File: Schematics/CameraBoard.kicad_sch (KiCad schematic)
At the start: 0 parts

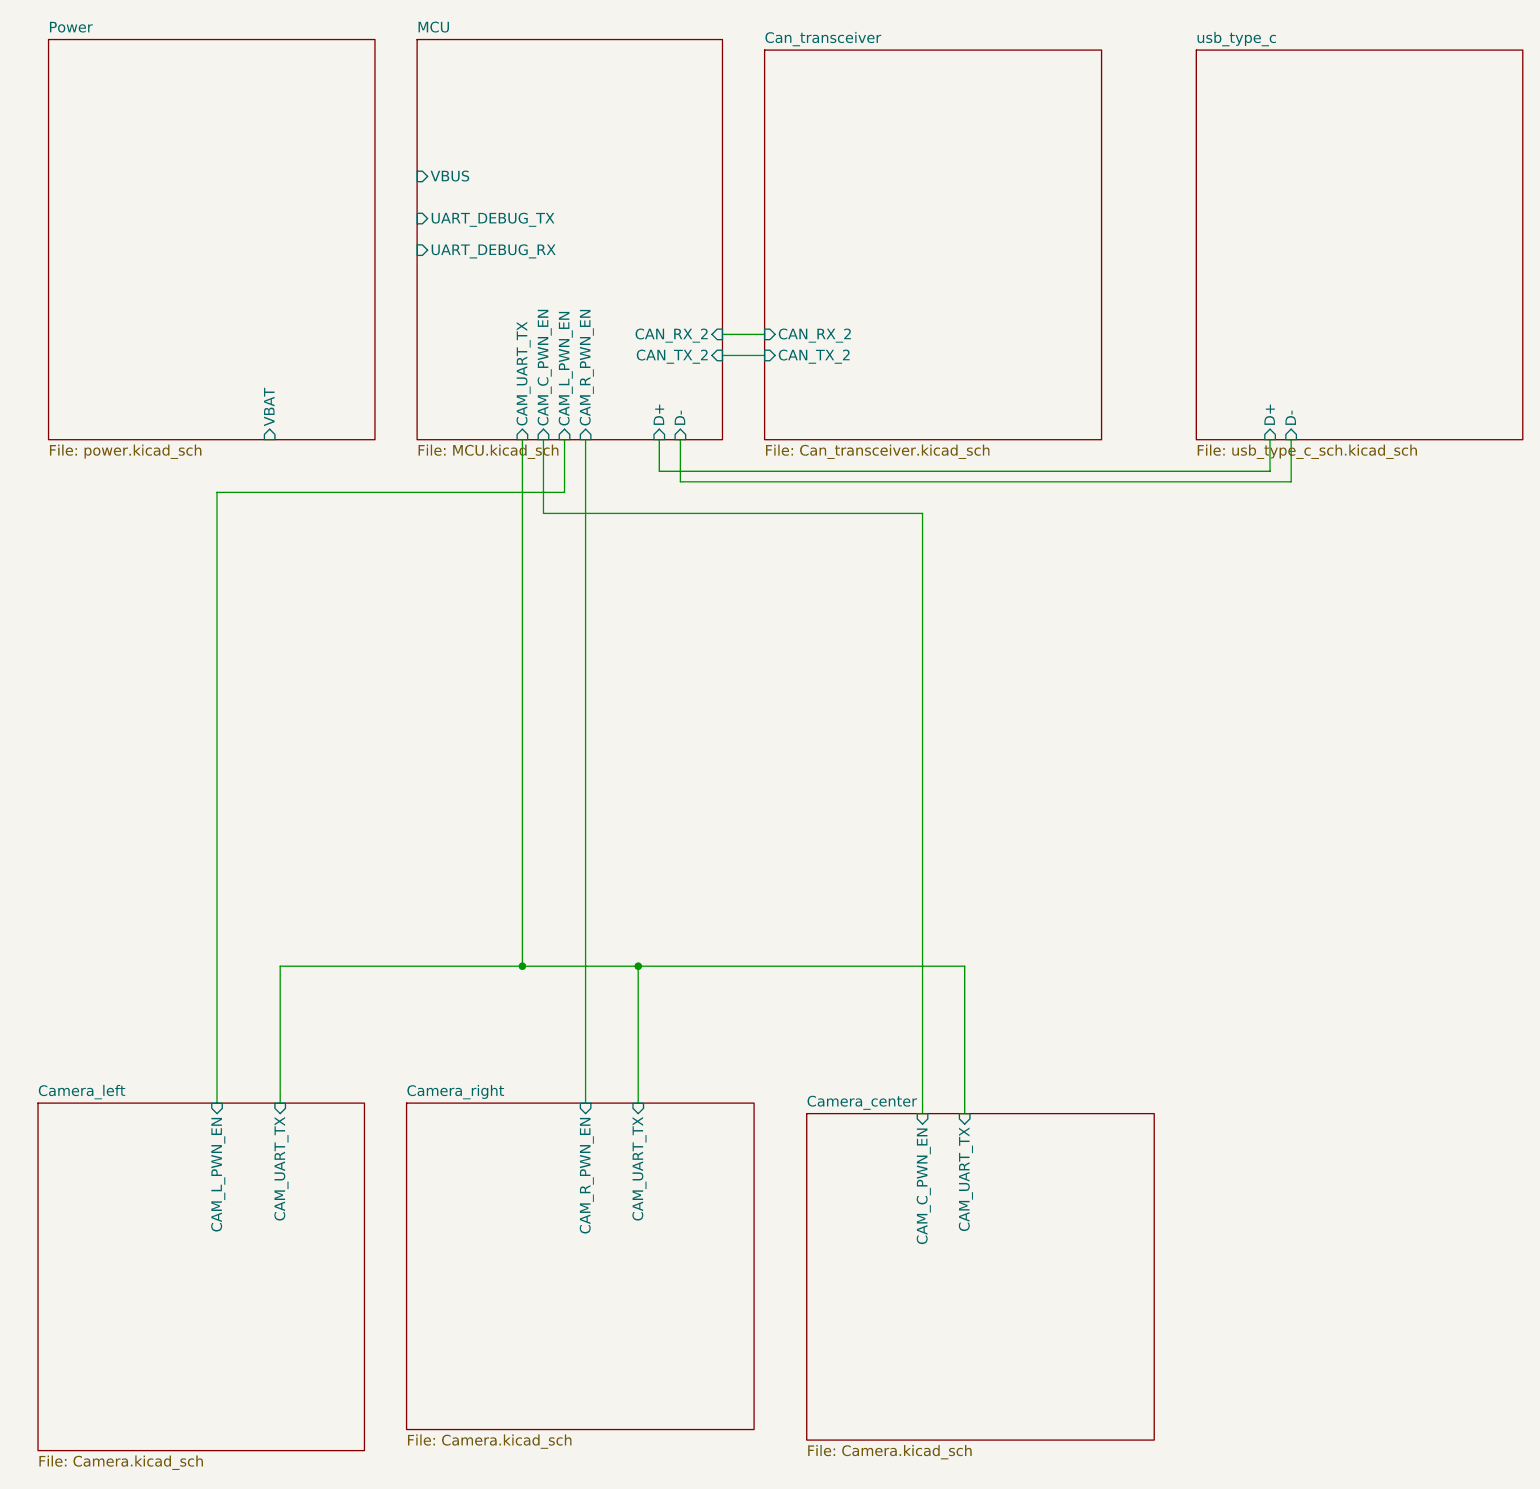
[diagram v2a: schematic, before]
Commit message: Ran ERC added Pwr Flags
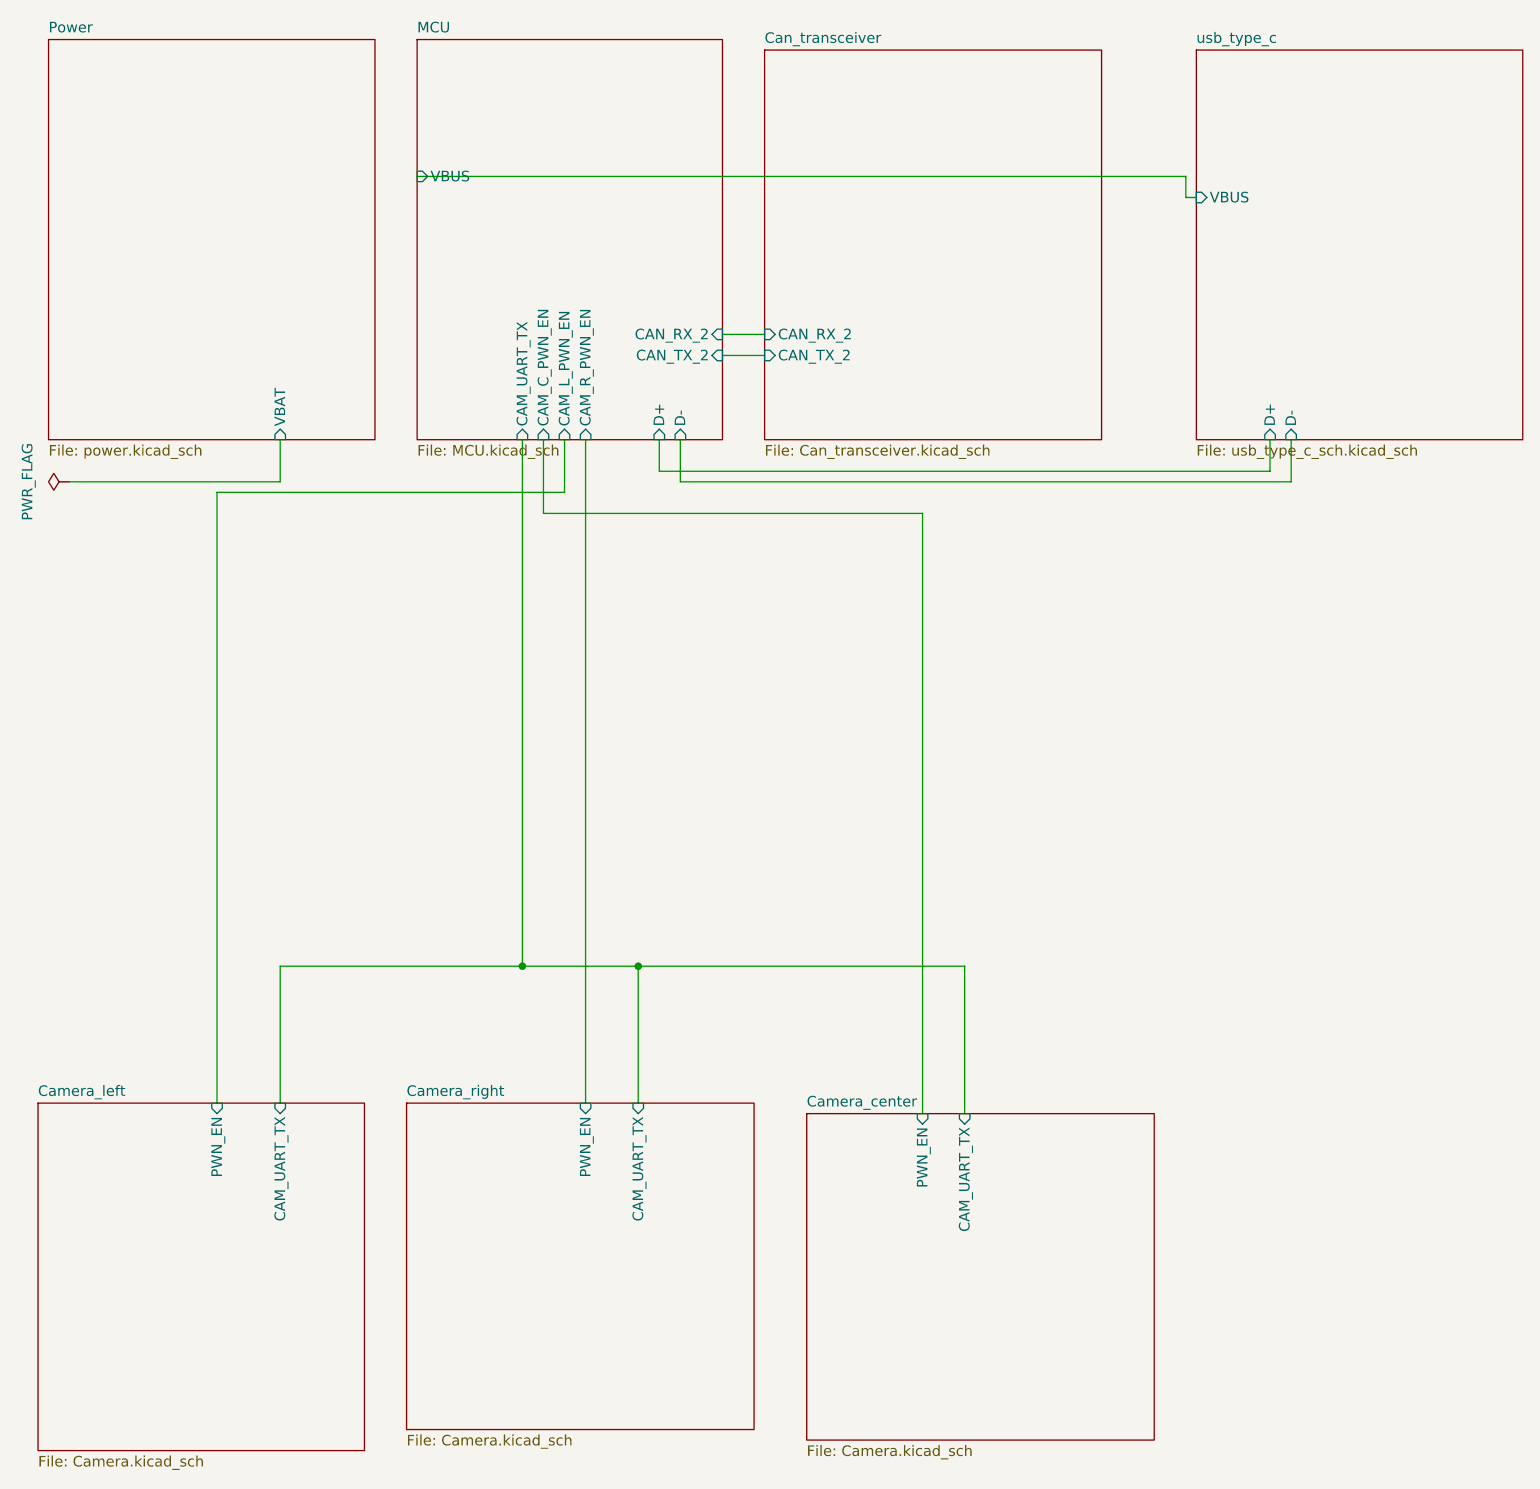
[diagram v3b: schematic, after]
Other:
- sheet Camera_center ports: added PWN_EN; removed CAM_C_PWN_EN
- sheet Camera_left ports: added PWN_EN; removed CAM_L_PWN_EN
- sheet Camera_right ports: added PWN_EN; removed CAM_R_PWN_EN
- sheet MCU ports: added none; removed UART_DEBUG_RX, UART_DEBUG_TX
- sheet usb_type_c ports: added VBUS; removed none
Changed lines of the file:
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@@
+	(wire
+		(pts
+			(xy 125.73 74.93) (xy 125.73 147.32)
+		)
+		(stroke
+			(width 0)
+			(type default)
+		)
+	)
+	(wire
+		(pts
+			(xy 48.26 71.12) (xy 48.26 66.04)
+		)
+		(stroke
+			(width 0)
+			(type default)
+		)
+	)
+	(wire
+		(pts
+			(xy 157.48 36.83) (xy 158.75 36.83)
+		)
+		(stroke
+			(width 0)
+			(type default)
+		)
+	)
 	(wire
 		(pts
@@
 	(wire
 		(pts
+			(xy 157.48 34.29) (xy 157.48 36.83)
+		)
+		(stroke
+			(width 0)
+			(type default)
+		)
+	)
+	(wire
+		(pts
 			(xy 93.98 66.04) (xy 93.98 69.85)
 		)
@@
 	(wire
 		(pts
-			(xy 125.73 147.32) (xy 125.73 74.93)
-		)
-		(stroke
-			(width 0)
-			(type default)
-		)
-	)
-	(wire
-		(pts
 			(xy 96.52 71.12) (xy 96.52 66.04)
 		)
@@
 	(wire
 		(pts
+			(xy 64.77 34.29) (xy 157.48 34.29)
+		)
+		(stroke
+			(width 0)
+			(type default)
+		)
+	)
+	(wire
+		(pts
 			(xy 40.64 146.05) (xy 40.64 72.39)
 		)
@@
 	(wire
 		(pts
+			(xy 22.86 71.12) (xy 48.26 71.12)
+		)
+		(stroke
+			(width 0)
+			(type default)
+		)
+	)
+	(wire
+		(pts
 			(xy 130.81 129.54) (xy 130.81 147.32)
 		)
@@
 			(width 0)
 			(type default)
+		)
+	)
+	(symbol
+		(lib_id "power:PWR_FLAG")
+		(at 22.86 71.12 90)
+		(unit 1)
+		(exclude_from_sim no)
+		(in_bom yes)
+		(on_board yes)
+		(dnp no)
+		(property "Reference" "#FLG01"
+			(at 20.955 71.12 0)
+			(effects
+				(font
+					(size 1.27 1.27)
+				)
+				(hide yes)
+			)
+		)
+		(property "Value" "PWR_FLAG"
+			(at 17.78 71.12 0)
+			(effects
+				(font
+					(size 1.27 1.27)
+				)
+			)
+		)
+		(property "Footprint" ""
+			(at 22.86 71.12 0)
+			(effects
+				(font
+					(size 1.27 1.27)
+				)
+				(hide yes)
+			)
+		)
+		(property "Datasheet" "~"
+			(at 22.86 71.12 0)
+			(effects
+				(font
+					(size 1.27 1.27)
+				)
+				(hide yes)
+			)
+		)
+		(property "Description" "Special symbol for telling ERC where power comes from"
+			(at 22.86 71.12 0)
+			(effects
+				(font
+					(size 1.27 1.27)
+				)
+				(hide yes)
+			)
+		)
+		(pin "1"
+		)
+		(instances
+			(project ""
+				(path "/65068a32-f105-4204-b50e-234054c5a6d0"
+					(reference "#FLG01")
+					(unit 1)
+				)
+			)
 		)
 	)
@@
 			)
 		)
-		(pin "CAM_C_PWN_EN" input
+		(pin "PWN_EN" input
 			(at 125.73 147.32 90)
 			(effects
@@
 		)
 		(pin "VBAT" input
-			(at 46.99 66.04 270)
+			(at 48.26 66.04 270)
 			(effects
 				(font
@@
 			)
 		)
-		(pin "UART_DEBUG_RX" input
-			(at 64.77 43.18 180)
-			(effects
-				(font
-					(size 1.27 1.27)
-				)
-				(justify left)
-			)
-		)
-		(pin "UART_DEBUG_TX" input
-			(at 64.77 39.37 180)
-			(effects
-				(font
-					(size 1.27 1.27)
-				)
-				(justify left)
-			)
-		)
 		(pin "VBUS" input
 			(at 64.77 34.29 180)
@@
 			)
 		)
-		(pin "CAM_R_PWN_EN" input
+		(pin "PWN_EN" input
 			(at 85.09 146.05 90)
 			(effects
@@
 			)
 		)
+		(pin "VBUS" input
+			(at 158.75 36.83 180)
+			(effects
+				(font
+					(size 1.27 1.27)
+				)
+				(justify left)
+			)
+		)
 		(instances
 			(project "CameraBoard"
@@
 			)
 		)
-		(pin "CAM_L_PWN_EN" input
+		(pin "PWN_EN" input
 			(at 40.64 146.05 90)
 			(effects

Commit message: final design pcb
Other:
- sheet Camera_center ports: added Cam5v; removed none
- sheet Camera_left ports: added Cam5v; removed none
- sheet Camera_right ports: added Cam5v; removed none
- sheet Power ports: added USB 5v; removed VBAT
- sheet usb_type_c ports: added USB 5v; removed none
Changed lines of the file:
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@@
+	)
+	(junction
+		(at 135.89 130.81)
+		(diameter 0)
+		(color 0 0 0 0)
 	)
 	(junction
@@
 		(color 0 0 0 0)
 	)
+	(junction
+		(at 135.89 139.7)
+		(diameter 0)
+		(color 0 0 0 0)
+	)
+	(junction
+		(at 97.79 139.7)
+		(diameter 0)
+		(color 0 0 0 0)
+	)
 	(wire
 		(pts
@@
 	(wire
 		(pts
+			(xy 135.89 125.73) (xy 135.89 130.81)
+		)
+		(stroke
+			(width 0)
+			(type default)
+		)
+	)
+	(wire
+		(pts
 			(xy 170.18 66.04) (xy 170.18 71.12)
 		)
@@
 	(wire
 		(pts
-			(xy 48.26 71.12) (xy 48.26 66.04)
+			(xy 97.79 139.7) (xy 97.79 146.05)
 		)
 		(stroke
@@
 	(wire
 		(pts
+			(xy 158.75 27.94) (xy 158.75 30.48)
+		)
+		(stroke
+			(width 0)
+			(type default)
+		)
+	)
+	(wire
+		(pts
 			(xy 85.09 66.04) (xy 85.09 146.05)
 		)
@@
 	(wire
 		(pts
+			(xy 137.16 139.7) (xy 137.16 147.32)
+		)
+		(stroke
+			(width 0)
+			(type default)
+		)
+	)
+	(wire
+		(pts
 			(xy 77.47 129.54) (xy 48.26 129.54)
 		)
@@
 	(wire
 		(pts
+			(xy 135.89 130.81) (xy 135.89 139.7)
+		)
+		(stroke
+			(width 0)
+			(type default)
+		)
+	)
+	(wire
+		(pts
 			(xy 96.52 71.12) (xy 96.52 66.04)
 		)
@@
 	(wire
 		(pts
+			(xy 59.69 27.94) (xy 158.75 27.94)
+		)
+		(stroke
+			(width 0)
+			(type default)
+		)
+	)
+	(wire
+		(pts
 			(xy 77.47 66.04) (xy 77.47 129.54)
 		)
@@
 	(wire
 		(pts
+			(xy 97.79 139.7) (xy 135.89 139.7)
+		)
+		(stroke
+			(width 0)
+			(type default)
+		)
+	)
+	(wire
+		(pts
 			(xy 93.98 69.85) (xy 167.64 69.85)
 		)
@@
 	(wire
 		(pts
+			(xy 34.29 139.7) (xy 97.79 139.7)
+		)
+		(stroke
+			(width 0)
+			(type default)
+		)
+	)
+	(wire
+		(pts
 			(xy 40.64 72.39) (xy 82.55 72.39)
 		)
@@
 	(wire
 		(pts
+			(xy 135.89 139.7) (xy 137.16 139.7)
+		)
+		(stroke
+			(width 0)
+			(type default)
+		)
+	)
+	(wire
+		(pts
+			(xy 34.29 146.05) (xy 34.29 139.7)
+		)
+		(stroke
+			(width 0)
+			(type default)
+		)
+	)
+	(wire
+		(pts
 			(xy 101.6 53.34) (xy 106.68 53.34)
 		)
@@
 	(wire
 		(pts
-			(xy 22.86 71.12) (xy 48.26 71.12)
-		)
-		(stroke
-			(width 0)
-			(type default)
-		)
-	)
-	(wire
-		(pts
 			(xy 130.81 129.54) (xy 130.81 147.32)
 		)
@@
 	)
 	(symbol
-		(lib_id "power:PWR_FLAG")
-		(at 22.86 71.12 90)
+		(lib_id "power:+5V")
+		(at 135.89 125.73 0)
 		(unit 1)
 		(exclude_from_sim no)
@@
 		(on_board yes)
 		(dnp no)
-		(property "Reference" "#FLG01"
-			(at 20.955 71.12 0)
+		(fields_autoplaced yes)
+		(property "Reference" "#PWR035"
+			(at 135.89 129.54 0)
 			(effects
 				(font
@@
 			)
 		)
-		(property "Value" "PWR_FLAG"
-			(at 17.78 71.12 0)
+		(property "Value" "+5V"
+			(at 135.89 120.65 0)
 			(effects
 				(font
@@
 		)
 		(property "Footprint" ""
-			(at 22.86 71.12 0)
+			(at 135.89 125.73 0)
 			(effects
 				(font
@@
 			)
 		)
-		(property "Datasheet" "~"
-			(at 22.86 71.12 0)
+		(property "Datasheet" ""
+			(at 135.89 125.73 0)
 			(effects
 				(font
@@
 			)
 		)
-		(property "Description" "Special symbol for telling ERC where power comes from"
-			(at 22.86 71.12 0)
+		(property "Description" "Power symbol creates a global label with name \"+5V\""
+			(at 135.89 125.73 0)
 			(effects
 				(font
@@
 			(project ""
 				(path "/65068a32-f105-4204-b50e-234054c5a6d0"
-					(reference "#FLG01")
+					(reference "#PWR035")
+					(unit 1)
+				)
+			)
+		)
+	)
+	(symbol
+		(lib_id "power:PWR_FLAG")
+		(at 135.89 130.81 270)
+		(unit 1)
+		(exclude_from_sim no)
+		(in_bom yes)
+		(on_board yes)
+		(dnp no)
+		(fields_autoplaced yes)
+		(property "Reference" "#FLG07"
+			(at 137.795 130.81 0)
+			(effects
+				(font
+					(size 1.27 1.27)
+				)
+				(hide yes)
+			)
+		)
+		(property "Value" "PWR_FLAG"
+			(at 139.7 130.8099 90)
+			(effects
+				(font
+					(size 1.27 1.27)
+				)
+				(justify left)
+			)
+		)
+		(property "Footprint" ""
+			(at 135.89 130.81 0)
+			(effects
+				(font
+					(size 1.27 1.27)
+				)
+				(hide yes)
+			)
+		)
+		(property "Datasheet" "~"
+			(at 135.89 130.81 0)
+			(effects
+				(font
+					(size 1.27 1.27)
+				)
+				(hide yes)
+			)
+		)
+		(property "Description" "Special symbol for telling ERC where power comes from"
+			(at 135.89 130.81 0)
+			(effects
+				(font
+					(size 1.27 1.27)
+				)
+				(hide yes)
+			)
+		)
+		(pin "1"
+		)
+		(instances
+			(project ""
+				(path "/65068a32-f105-4204-b50e-234054c5a6d0"
+					(reference "#FLG07")
 					(unit 1)
 				)
@@
 			)
 		)
+		(pin "Cam5v" input
+			(at 137.16 147.32 90)
+			(effects
+				(font
+					(size 1.27 1.27)
+				)
+				(justify right)
+			)
+		)
 		(instances
 			(project "CameraBoard"
@@
 			)
 		)
-		(pin "VBAT" input
-			(at 48.26 66.04 270)
-			(effects
-				(font
-					(size 1.27 1.27)
-				)
-				(justify left)
+		(pin "USB 5v" input
+			(at 59.69 27.94 0)
+			(effects
+				(font
+					(size 1.27 1.27)
+				)
+				(justify right)
 			)
 		)
@@
 			)
 		)
+		(pin "Cam5v" input
+			(at 97.79 146.05 90)
+			(effects
+				(font
+					(size 1.27 1.27)
+				)
+				(justify right)
+			)
+		)
 		(instances
 			(project "CameraBoard"
@@
 			)
 		)
+		(pin "USB 5v" input
+			(at 158.75 30.48 180)
+			(effects
+				(font
+					(size 1.27 1.27)
+				)
+				(justify left)
+			)
+		)
 		(instances
 			(project "CameraBoard"
@@
 			(effects
 				(font
+					(size 1.27 1.27)
+				)
+				(justify right)
+			)
+		)
+		(pin "Cam5v" input
+			(at 34.29 146.05 90)
+			(effects
+				(font
